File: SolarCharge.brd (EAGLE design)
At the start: 63 x 63 mm, 20 parts, among them U1 TINY4/5/9/10-TSHR/TS8R, U2 TINY4/5/9/10-TSHR/TS8R

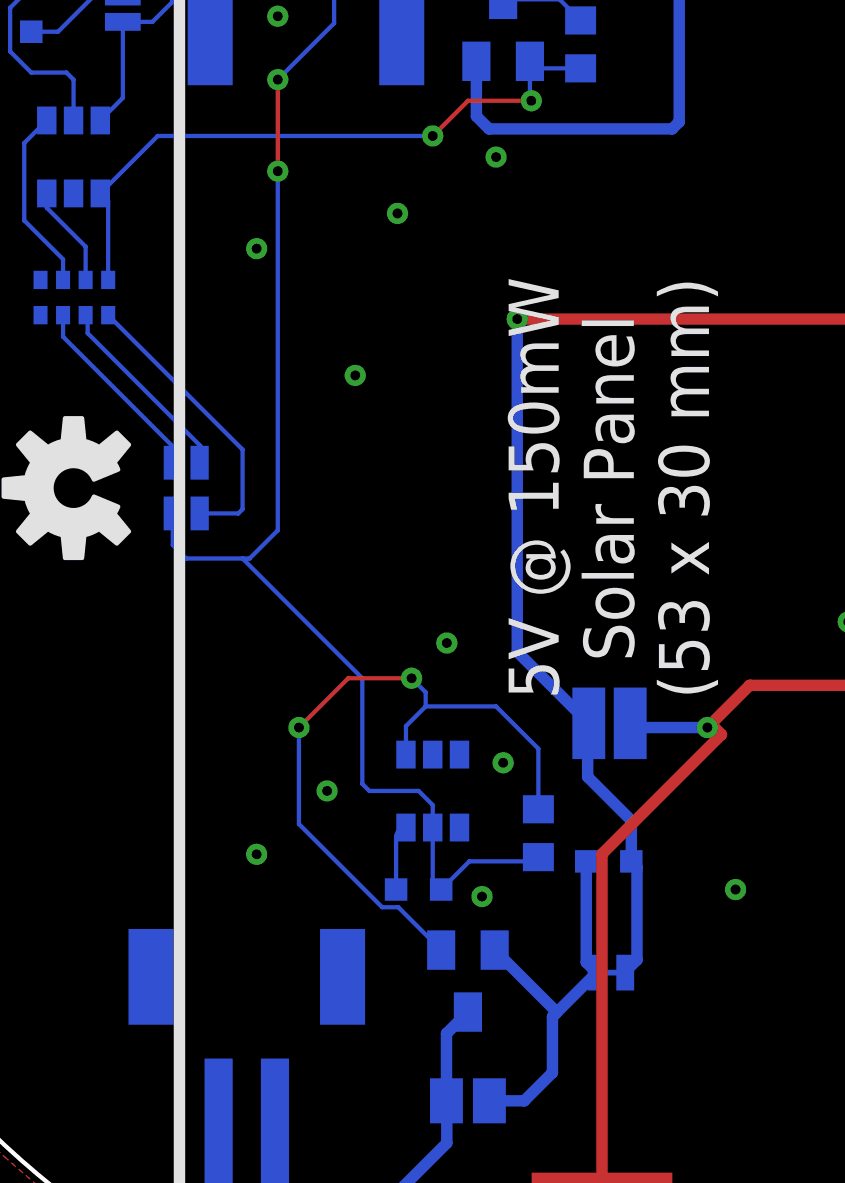
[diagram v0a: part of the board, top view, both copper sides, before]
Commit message: Solar out to 3V3 solderjumper
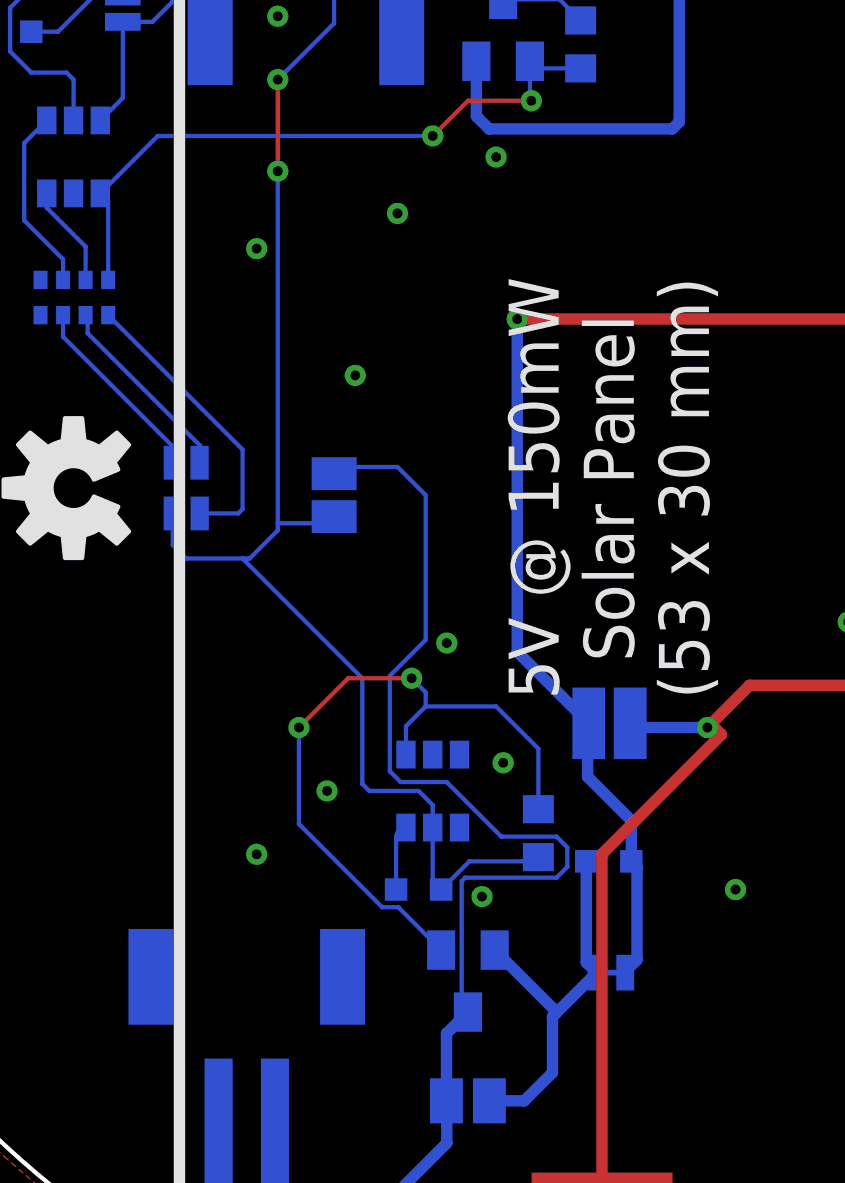
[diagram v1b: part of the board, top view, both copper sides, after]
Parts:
- added SJ3: (no value), jumper:SJ
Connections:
- net +3V3: now also SJ3.2
- net N$9: now also SJ3.1
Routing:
- net N$9: track 18.1 -> 49.0 mm
- net +3V3: track 84.0 -> 86.1 mm
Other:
- board text added: "Solar out to 3V3"
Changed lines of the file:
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@@
 <layer number="20" name="Dimension" color="24" fill="1" visible="no" active="yes"/>
 <layer number="21" name="tPlace" color="7" fill="1" visible="yes" active="yes"/>
-<layer number="22" name="bPlace" color="7" fill="1" visible="no" active="yes"/>
-<layer number="23" name="tOrigins" color="15" fill="1" visible="no" active="yes"/>
-<layer number="24" name="bOrigins" color="15" fill="1" visible="no" active="yes"/>
+<layer number="22" name="bPlace" color="7" fill="1" visible="yes" active="yes"/>
+<layer number="23" name="tOrigins" color="15" fill="1" visible="yes" active="yes"/>
+<layer number="24" name="bOrigins" color="15" fill="1" visible="yes" active="yes"/>
 <layer number="25" name="tNames" color="7" fill="1" visible="no" active="yes"/>
 <layer number="26" name="bNames" color="7" fill="1" visible="no" active="yes"/>
@@
 <wire x1="25.25" y1="60.225" x2="28.25" y2="60.225" width="0.4064" layer="22"/>
 <dimension x1="20.25" y1="62.75" x2="20" y2="-0.25" x3="61.22455" y3="31.086903125" textsize="1.778" layer="47" dtype="diameter"/>
+<text x="13.5" y="31.5" size="1.016" layer="22" rot="SMR270" align="center">Solar out
+to 3V3</text>
 </plain>
 <attributes>
@@
 <attribute name="VALUE" x="15.0999" y="9.75" size="0.02" layer="28" rot="MR0"/>
 </element>
+<element name="SJ3" library="jumper" library_urn="urn:adsk.eagle:library:252" package="SJ" package3d_urn="urn:adsk.eagle:package:15471/1" value="" x="10.75" y="31.25" smashed="yes" rot="MR270">
+<attribute name="NAME" x="9.607" y="32.901" size="1.27" layer="26" ratio="10" rot="MR270"/>
+<attribute name="VALUE" x="10.75" y="30.8499" size="0.02" layer="28" rot="MR270"/>
+</element>
 </elements>
 <signals>
@@
 <contactref element="R4" pad="2"/>
 <contactref element="R5" pad="1"/>
-<wire x1="8.75" y1="30" x2="8.75" y2="42.75" width="0.1524" layer="16"/>
+<wire x1="8.75" y1="30" x2="8.75" y2="30.25" width="0.1524" layer="16"/>
 <via x="8.75" y="42.75" extent="1-16" drill="0.35"/>
 <via x="8.75" y="46" extent="1-16" drill="0.35"/>
+<wire x1="8.75" y1="30.25" x2="8.75" y2="42.75" width="0.1524" layer="16"/>
 <wire x1="8.75" y1="42.75" x2="8.75" y2="46" width="0.1524" layer="1"/>
-<wire x1="14.25" y1="19.45" x2="14.25" y2="19.25" width="0.1524" layer="16"/>
-<wire x1="14.25" y1="19.25" x2="14.25" y2="17.25" width="0.1524" layer="16"/>
+<wire x1="14.25" y1="19.45" x2="14.25" y2="17.25" width="0.1524" layer="16"/>
 <wire x1="14.25" y1="17.25" x2="14.55" y2="17.25" width="0.1524" layer="16"/>
 <wire x1="14.55" y1="17.25" x2="15.55" y2="18.25" width="0.1524" layer="16"/>
@@
 <wire x1="13.75" y1="20.75" x2="14.25" y2="20.25" width="0.1524" layer="16"/>
 <wire x1="14.25" y1="20.25" x2="14.25" y2="19.45" width="0.1524" layer="16"/>
+<contactref element="SJ3" pad="2"/>
+<wire x1="10.75" y1="30.488" x2="10.512" y2="30.25" width="0.1524" layer="16"/>
+<wire x1="10.512" y1="30.25" x2="8.75" y2="30.25" width="0.1524" layer="16"/>
 </signal>
 <signal name="RED_RESISTOR">
@@
 <vertex x="20.75" y="56.5"/>
 </polygon>
-</signal>
-<signal name="N$9">
-<contactref element="CN1" pad="1"/>
-<contactref element="Q2" pad="3"/>
-<contactref element="SJ4" pad="2"/>
-<wire x1="15.5" y1="12.9" x2="14.738" y2="12.138" width="0.4064" layer="16"/>
-<wire x1="14.738" y1="12.138" x2="14.738" y2="9.75" width="0.4064" layer="16"/>
-<wire x1="6.65" y1="8.95" x2="6.65" y2="5.85" width="0.4064" layer="16"/>
-<wire x1="6.65" y1="5.85" x2="7.75" y2="4.75" width="0.4064" layer="16"/>
-<wire x1="7.75" y1="4.75" x2="11.25" y2="4.75" width="0.4064" layer="16"/>
-<wire x1="11.25" y1="4.75" x2="14.75" y2="8.25" width="0.4064" layer="16"/>
-<wire x1="14.75" y1="8.25" x2="14.75" y2="9.738" width="0.4064" layer="16"/>
-<wire x1="14.75" y1="9.738" x2="14.738" y2="9.75" width="0.4064" layer="16"/>
 </signal>
 <signal name="N$10">
@@
 <wire x1="12.95" y1="19.1" x2="12.95" y2="17.25" width="0.1524" layer="16"/>
 </signal>
+<signal name="N$9">
+<contactref element="CN1" pad="1"/>
+<contactref element="Q2" pad="3"/>
+<contactref element="SJ4" pad="2"/>
+<wire x1="15.5" y1="12.9" x2="14.738" y2="12.138" width="0.4064" layer="16"/>
+<wire x1="14.738" y1="12.138" x2="14.738" y2="9.75" width="0.4064" layer="16"/>
+<wire x1="6.65" y1="8.95" x2="6.65" y2="5.85" width="0.4064" layer="16"/>
+<wire x1="6.65" y1="5.85" x2="7.75" y2="4.75" width="0.4064" layer="16"/>
+<wire x1="7.75" y1="4.75" x2="11.25" y2="4.75" width="0.4064" layer="16"/>
+<wire x1="11.25" y1="4.75" x2="14.75" y2="8.25" width="0.4064" layer="16"/>
+<wire x1="14.75" y1="8.25" x2="14.75" y2="9.738" width="0.4064" layer="16"/>
+<wire x1="14.75" y1="9.738" x2="14.738" y2="9.75" width="0.4064" layer="16"/>
+<contactref element="SJ3" pad="1"/>
+<wire x1="10.75" y1="32.012" x2="10.988" y2="32.25" width="0.1524" layer="16"/>
+<wire x1="10.988" y1="32.25" x2="13" y2="32.25" width="0.1524" layer="16"/>
+<wire x1="14" y1="31.25" x2="13" y2="32.25" width="0.1524" layer="16"/>
+<wire x1="18.6446875" y1="17.6714" x2="19.0286" y2="18.0553125" width="0.1524" layer="16"/>
+<wire x1="19.0286" y1="18.0553125" x2="19.0286" y2="18.7446875" width="0.1524" layer="16"/>
+<wire x1="19.0286" y1="18.7446875" x2="18.6446875" y2="19.1286" width="0.1524" layer="16"/>
+<wire x1="13.1103125" y1="21.0664" x2="12.7264" y2="21.4503125" width="0.1524" layer="16"/>
+<wire x1="15.5" y1="12.9" x2="15.2786" y2="13.1214" width="0.1524" layer="16"/>
+<wire x1="14" y1="26.10815" x2="14" y2="31.25" width="0.1524" layer="16"/>
+<wire x1="15.40245625" y1="17.6714" x2="18.6446875" y2="17.6714" width="0.1524" layer="16"/>
+<wire x1="14.7468875" y1="21.0664" x2="13.1103125" y2="21.0664" width="0.1524" layer="16"/>
+<wire x1="15.2786" y1="17.54754375" x2="15.40245625" y2="17.6714" width="0.1524" layer="16"/>
+<wire x1="15.2786" y1="13.1214" x2="15.2786" y2="17.54754375" width="0.1524" layer="16"/>
+<wire x1="18.6446875" y1="19.1286" x2="16.6846875" y2="19.1286" width="0.1524" layer="16"/>
+<wire x1="16.6846875" y1="19.1286" x2="14.7468875" y2="21.0664" width="0.1524" layer="16"/>
+<wire x1="12.7264" y1="21.4503125" x2="12.7264" y2="24.83455" width="0.1524" layer="16"/>
+<wire x1="12.7264" y1="24.83455" x2="14" y2="26.10815" width="0.1524" layer="16"/>
+</signal>
 </signals>

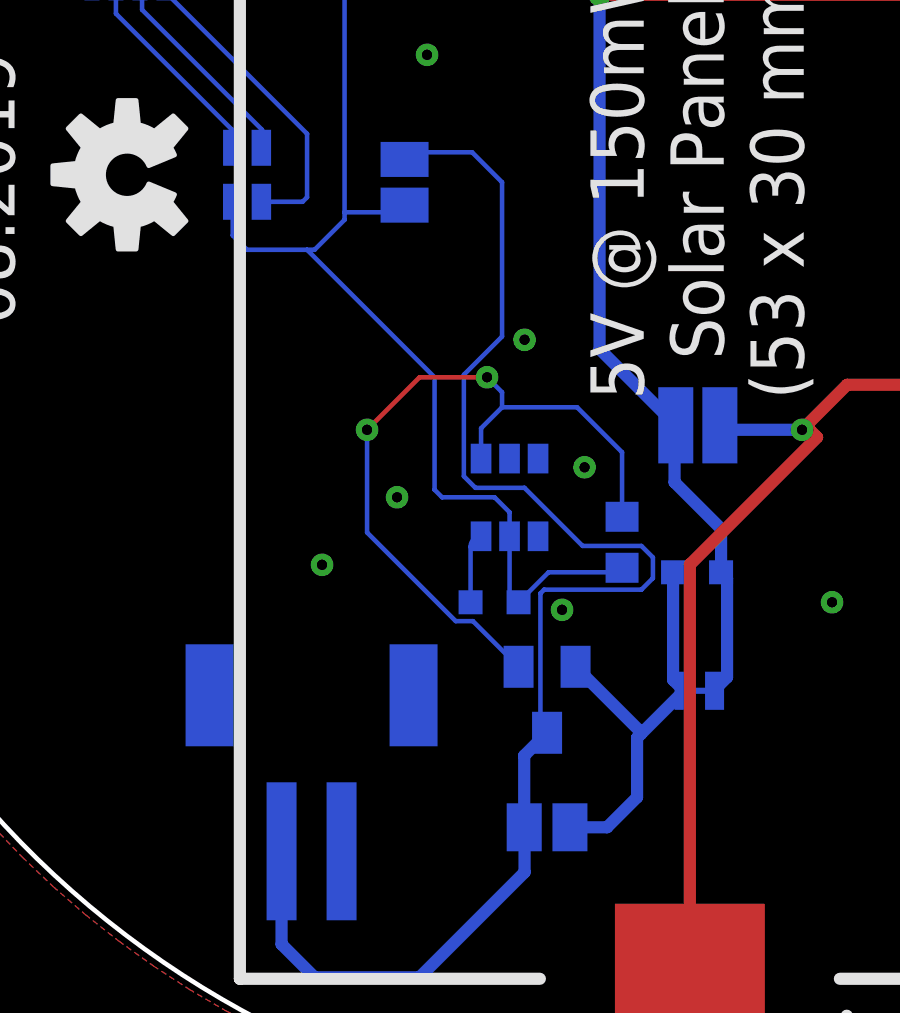
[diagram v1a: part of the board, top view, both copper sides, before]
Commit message: Use XC2606 LDO instead of Tiny10
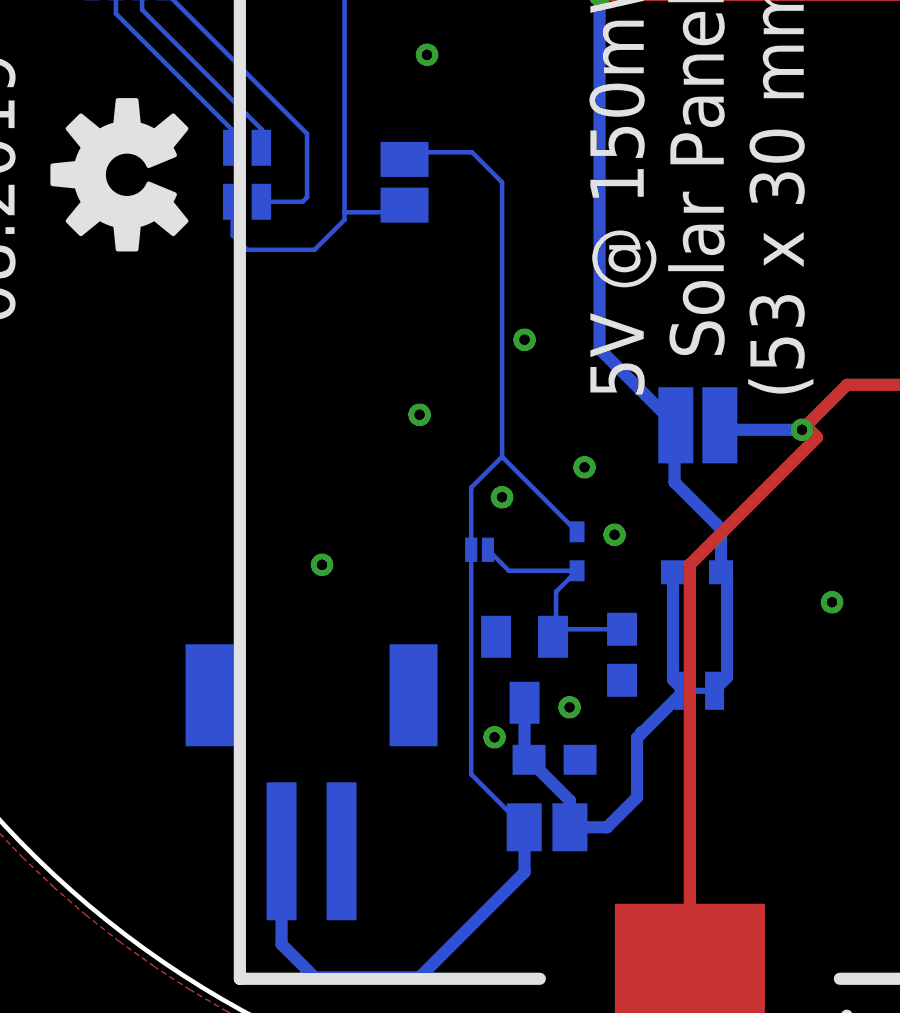
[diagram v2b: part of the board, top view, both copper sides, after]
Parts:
- removed Q2: (no value), adafruit:SOT23
- removed R4: (no value), rcl:R0603
- removed R5: (no value), ROHM:0603-RES
- removed U2: TINY4/5/9/10-TSHR/TS8R, bt_avr:SOT-23-6
- added C1, C9: 1uF, rcl:C0603
- added D6: 0.3V Schottky, diode:SOD523
- added IC2: (no value), MCP1700:SOT-23
- added J1: (no value), solderjumper:2.MED
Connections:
- removed net N$10: Q2.1, R4.1, U2.1
- removed net N$11: R5.2, U2.6
- removed net N$9: CN1.1, Q2.3, SJ3.1, SJ4.2
- new net +5V: C9.1, IC2.3, R1.2, SJ1.2, SJ4.1
- new net N$25: C1.1, D6.A, IC2.2, J1.1
- net +3V3: no longer R4.2, R5.1, U2.5
- net GND: now also C1.2, C9.2, IC2.1; no longer U2.2
- net N$4: now also CN1.1, D6.C, J1.2, SJ3.1, SJ4.2; no longer Q2.2, R1.2, SJ1.2, SJ4.1
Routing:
- net N$9: track 49.0 -> 0.00 mm
- net N$4: track 14.1 -> 44.6 mm
- net N$10: track 25.0 -> 0.00 mm, vias 2 -> 0
- net +3V3: track 86.1 -> 66.3 mm
- net +5V: track 0.00 -> 15.8 mm
- net N$25: track 0.00 -> 8.05 mm
- net N$11: track 2.34 -> 0.00 mm
- net GND: vias 17 -> 20
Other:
- board text added: "LDO bypass"
- board text added: "Led bypass"
- board text added: "Schottky bypass"

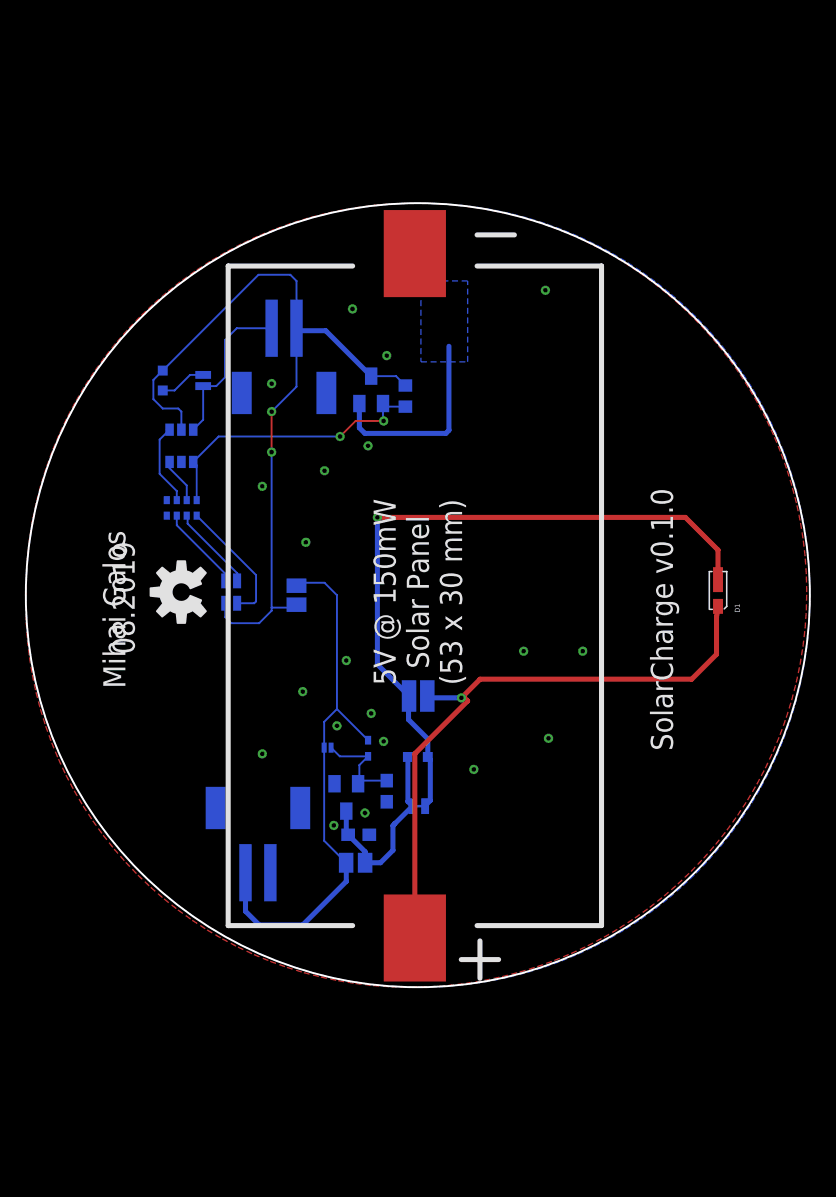
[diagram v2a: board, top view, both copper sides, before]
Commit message: Use ellipse for circle in dim layer, slanted facing sun
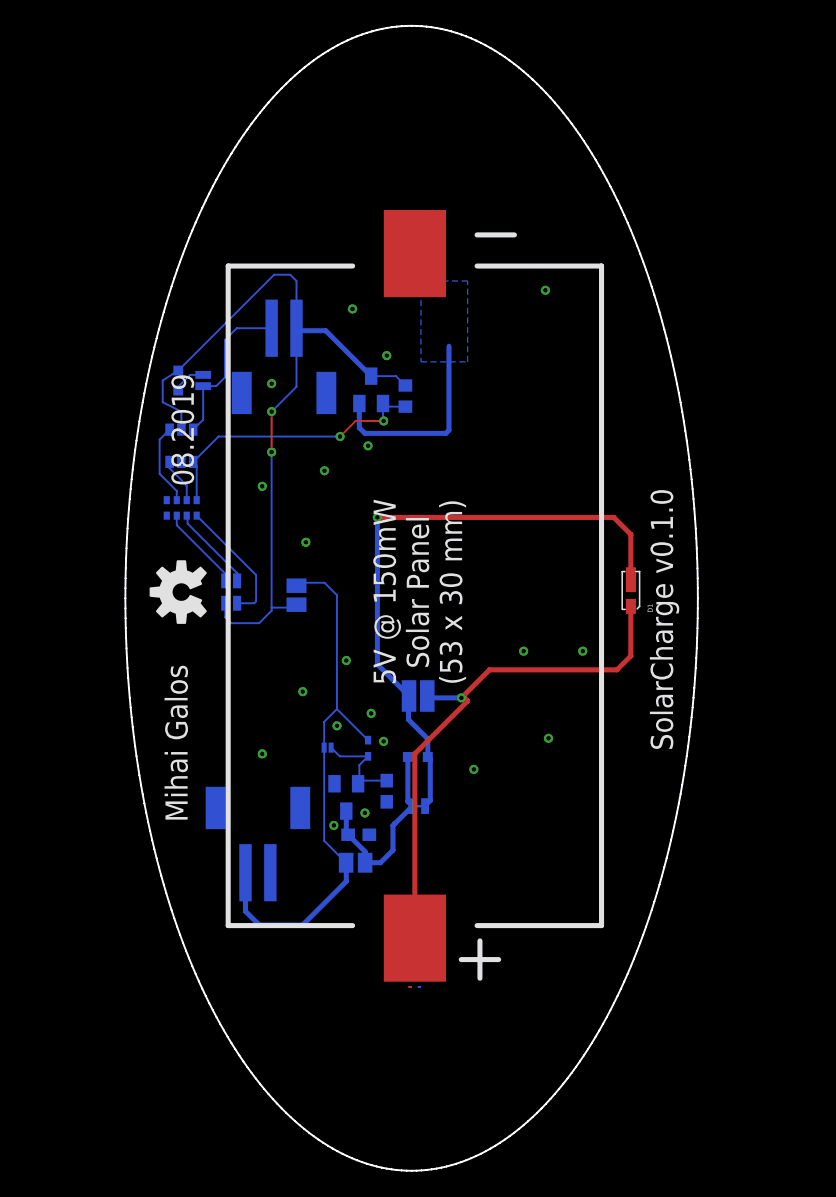
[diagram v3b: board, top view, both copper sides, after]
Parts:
- moved D1 7.00 mm to (37.6, 30.4)
- moved R2 1.25 mm to (1.25, 48.5)
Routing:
- net N$1: track 50.0 -> 43.2 mm
- net N$3: track 56.0 -> 49.7 mm
- net +3V3: track 66.3 -> 64.7 mm
- net N$7: track 3.77 -> 2.69 mm
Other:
- board size 63 x 63 mm -> 46 x 92 mm
